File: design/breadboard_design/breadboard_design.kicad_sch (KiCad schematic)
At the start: 11 parts, among them M1 STM32G041F8P6 Dev, SW1 Up, SW2 Enter, SW3 Down

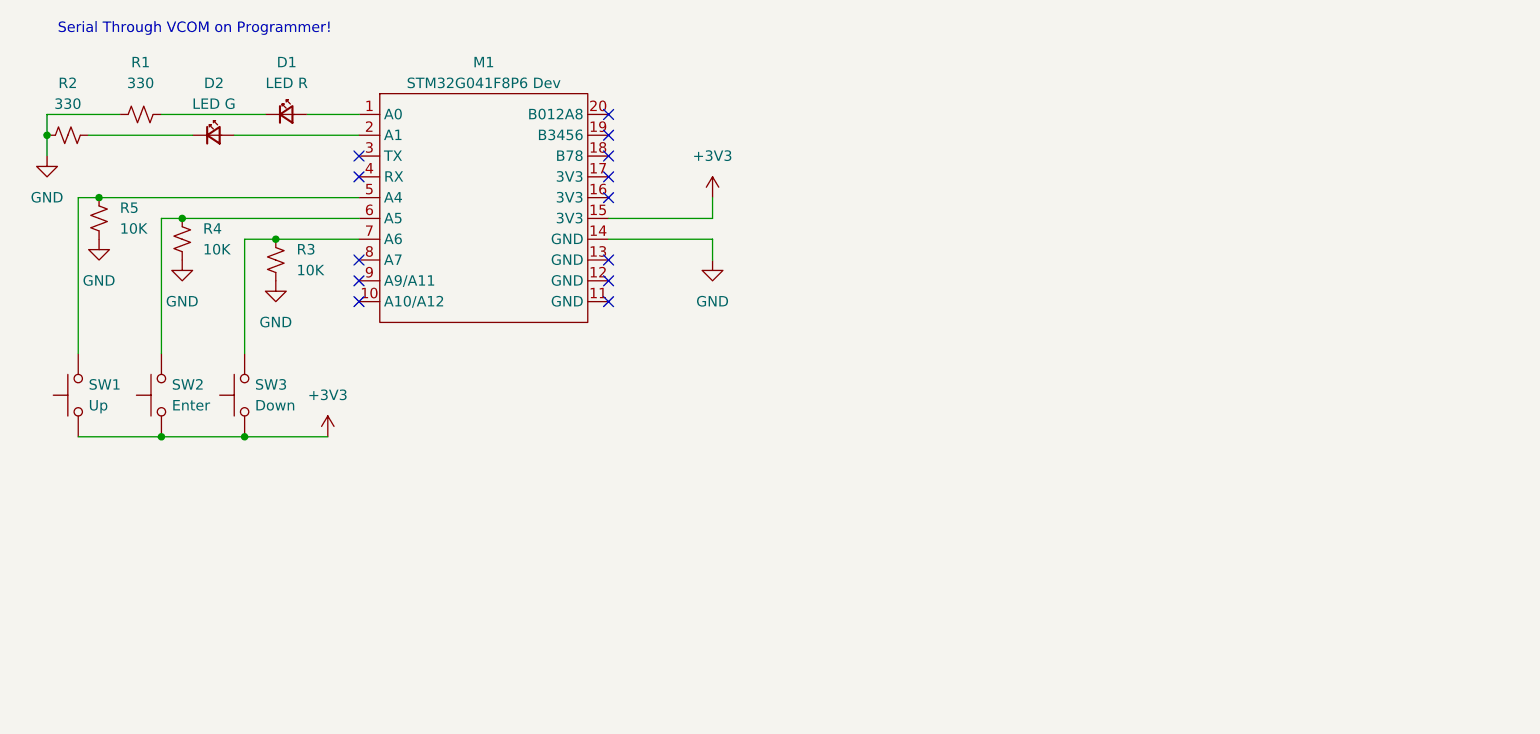
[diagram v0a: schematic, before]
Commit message: updates to breadboard demo
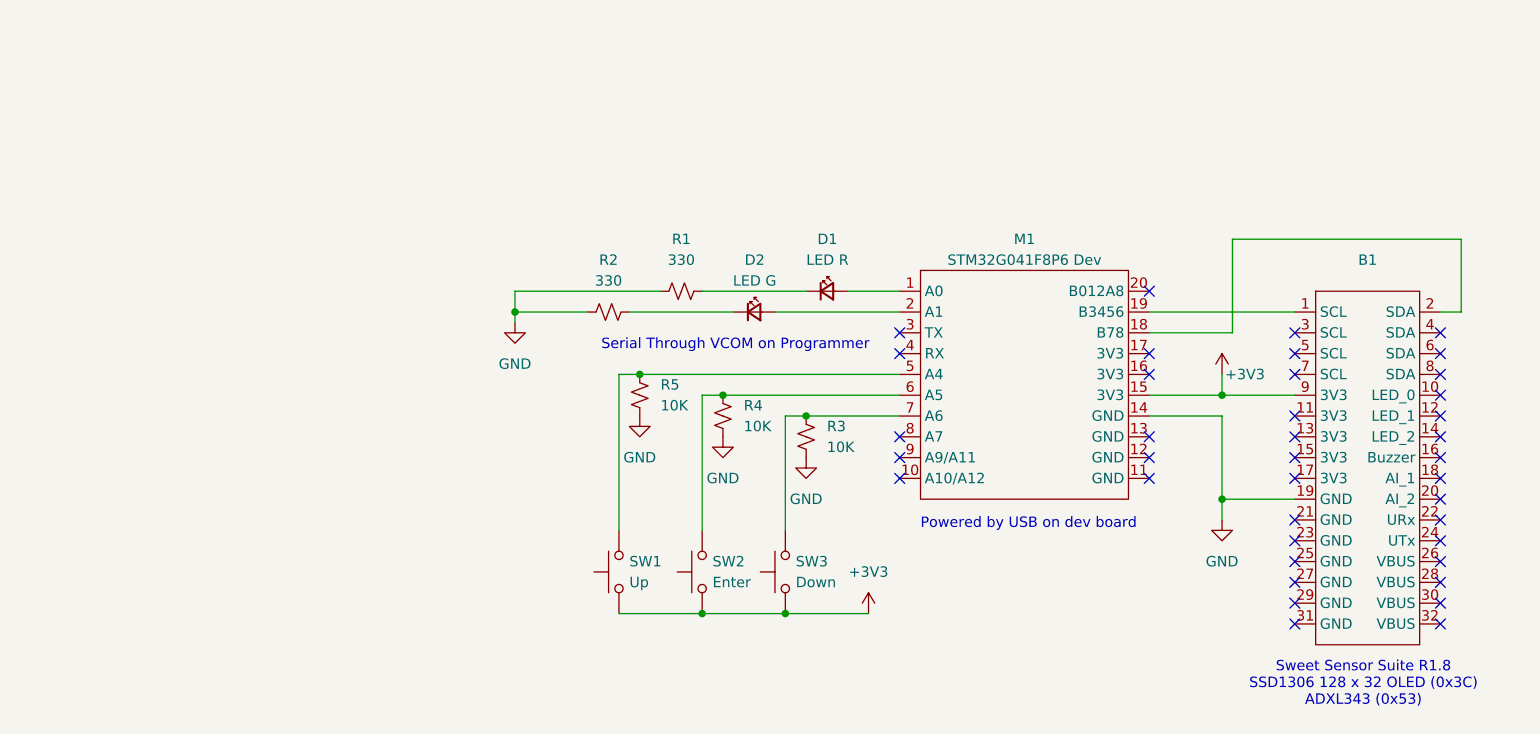
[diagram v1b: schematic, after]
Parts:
- added B1: ~, symbol simon_dev_g041:SSSR1_8
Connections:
- net +3V3: now also B1.9 (3V3)
- net GND: now also B1.19 (GND)
- net at M1.18 (B78): now also B1.2 (SDA)
- net at M1.19 (B3456): now also B1.1 (SCL)
- no-connect marks 13 -> 39
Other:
- note added: "Powered by USB on dev board"
- note added: "Serial Through VCOM on Programmer"
- note added: "Sweet Sensor Suite R1.8 SSD1306 128 x 32 OLED (0x3C) ADXL343 (0x53)"
- note removed: "Serial Through VCOM on Programmer!"
- company: (none) -> NAIT
- title: (none) -> Breadboard Design (Proof of life/early development)
- moved on the sheet: D1, D2, M1, R1, R2, R3, R4, R5, SW1, SW2, SW3

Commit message: added interrupt line to micro from SSSR1.8
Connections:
- net at M1.8 (A7): now also B1.18 (AI_1)
- no-connect marks 39 -> 37
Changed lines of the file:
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@@
-	)
-	(no_connect
-		(at 128.27 100.33)
-	)
-	(no_connect
-		(at 194.31 105.41)
 	)
 	(no_connect
@@
 	(wire
 		(pts
+			(xy 125.73 113.03) (xy 156.21 113.03)
+		)
+		(stroke
+			(width 0)
+			(type default)
+		)
+	)
+	(wire
+		(pts
 			(xy 128.27 92.71) (xy 96.52 92.71)
 		)
@@
 	(wire
 		(pts
+			(xy 204.47 134.62) (xy 204.47 105.41)
+		)
+		(stroke
+			(width 0)
+			(type default)
+		)
+	)
+	(wire
+		(pts
 			(xy 167.64 97.79) (xy 167.64 107.95)
 		)
@@
 	(wire
 		(pts
+			(xy 128.27 100.33) (xy 125.73 100.33)
+		)
+		(stroke
+			(width 0)
+			(type default)
+		)
+	)
+	(wire
+		(pts
 			(xy 167.64 92.71) (xy 167.64 95.25)
 		)
@@
 	(wire
 		(pts
+			(xy 156.21 113.03) (xy 156.21 134.62)
+		)
+		(stroke
+			(width 0)
+			(type default)
+		)
+	)
+	(wire
+		(pts
 			(xy 196.85 85.09) (xy 196.85 76.2)
 		)
@@
 	(wire
 		(pts
+			(xy 125.73 100.33) (xy 125.73 113.03)
+		)
+		(stroke
+			(width 0)
+			(type default)
+		)
+	)
+	(wire
+		(pts
 			(xy 158.75 95.25) (xy 167.64 95.25)
 		)
@@
 	(wire
 		(pts
+			(xy 204.47 105.41) (xy 194.31 105.41)
+		)
+		(stroke
+			(width 0)
+			(type default)
+		)
+	)
+	(wire
+		(pts
 			(xy 104.14 95.25) (xy 104.14 111.76)
 		)
@@
 		)
 		(stroke
+			(width 0)
+			(type default)
+		)
+	)
+	(wire
+		(pts
+			(xy 156.21 134.62) (xy 204.47 134.62)
+		)
+		(stroke
